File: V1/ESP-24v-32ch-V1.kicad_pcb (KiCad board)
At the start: 2 copper layers, 193 x 67.8 mm, 450 parts, among them J1 Conn_01x08, J10 USB, J11 ETHERNET, J2 Conn_01x08, J3 Conn_01x08, J4 Conn_01x08, J5 Conn_01x08, J6 Conn_01x08, J7 Conn_01x08, J8 Conn_01x08, J9 VIN, Q1 WPM2015-3/TR, Q10 MMBT2222A/SOT-23-3, Q11 MMBT2222A/SOT-23-3, Q12 MMBT2222A/SOT-23-3, Q13 MMBT2222A/SOT-23-3, Q14 MMBT2222A/SOT-23-3, Q15 MMBT2222A/SOT-23-3, Q16 MMBT2222A/SOT-23-3, Q17 MMBT2222A/SOT-23-3, Q18 MMBT2222A/SOT-23-3, Q19 MMBT2222A/SOT-23-3, Q2 LMUN2211LT1G, Q20 MMBT2222A/SOT-23-3, Q21 MMBT2222A/SOT-23-3, Q22 MMBT2222A/SOT-23-3, Q23 MMBT2222A/SOT-23-3, Q24 MMBT2222A/SOT-23-3, Q25 MMBT2222A/SOT-23-3, Q26 MMBT2222A/SOT-23-3, Q27 MMBT2222A/SOT-23-3, Q28 MMBT2222A/SOT-23-3, Q29 MMBT2222A/SOT-23-3, Q3 UMH3N, Q30 MMBT2222A/SOT-23-3, Q31 MMBT2222A/SOT-23-3, Q32 MMBT2222A/SOT-23-3, Q33 MMBT2222A/SOT-23-3, Q34 MMBT2222A/SOT-23-3, Q35 MMBT2222A/SOT-23-3, Q4 MMBT2222A/SOT-23-3, Q5 MMBT2222A/SOT-23-3, Q6 MMBT2222A/SOT-23-3, Q7 MMBT2222A/SOT-23-3, Q8 MMBT2222A/SOT-23-3, Q9 MMBT2222A/SOT-23-3, SW1 RESET, U1 SY8089A1AAC, U10 OR-3H4-4, U11 OR-3H4-4, U12 OR-3H4-4, U13 OR-3H4-4, U14 OR-3H4-4, U15 OR-3H4-4, U16 OR-3H4-4, U17 OR-3H4-4, U2 TX4138, U3 CH340C, U4 ESP32-WROOM-32UE-N16, U5 LAN8710A, U6 MCP23017_SS, U7 MCP23017_SS, U8 MCP23017_SS, U9 MCP23017_SS

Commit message: Dev
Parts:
- added REF**: OSHW-Logo2_9.8x8mm_SilkScreen, Symbol:OSHW-Logo2_9.8x8mm_SilkScreen, F.Cu at (172.7, 78.1)
- C1, C5: value 10uF/16V/1206 -> 10uF/50V/1206
- C11, C16, C17, C6, C9: value 10uF/6,3V/0603 -> 10uF/10V/0603
- C13: value 1uF/10V/0603 -> 1uF/50V/0603
- C15, C18, C19, C20: value 0,1uF/16V/0402 -> 0,1uF/50V/0402
- C21: value 1uF/6,3V/0402 -> 1uF/25V/0402
- C22: value 470pF/16V/0402 -> 470pF/50V/0402

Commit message: Replaced connector footprints
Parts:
- J1, J2, J3, J4, J5, J6, J7, J8: footprint Tales:TerminalBlock_Dorabo_DB141V-2.54-08P_1x08_P2.54mm_Vertical -> Tales:TerminalBlock_DG141V-2.54-8P_1x08_P2.54mm_Vertical

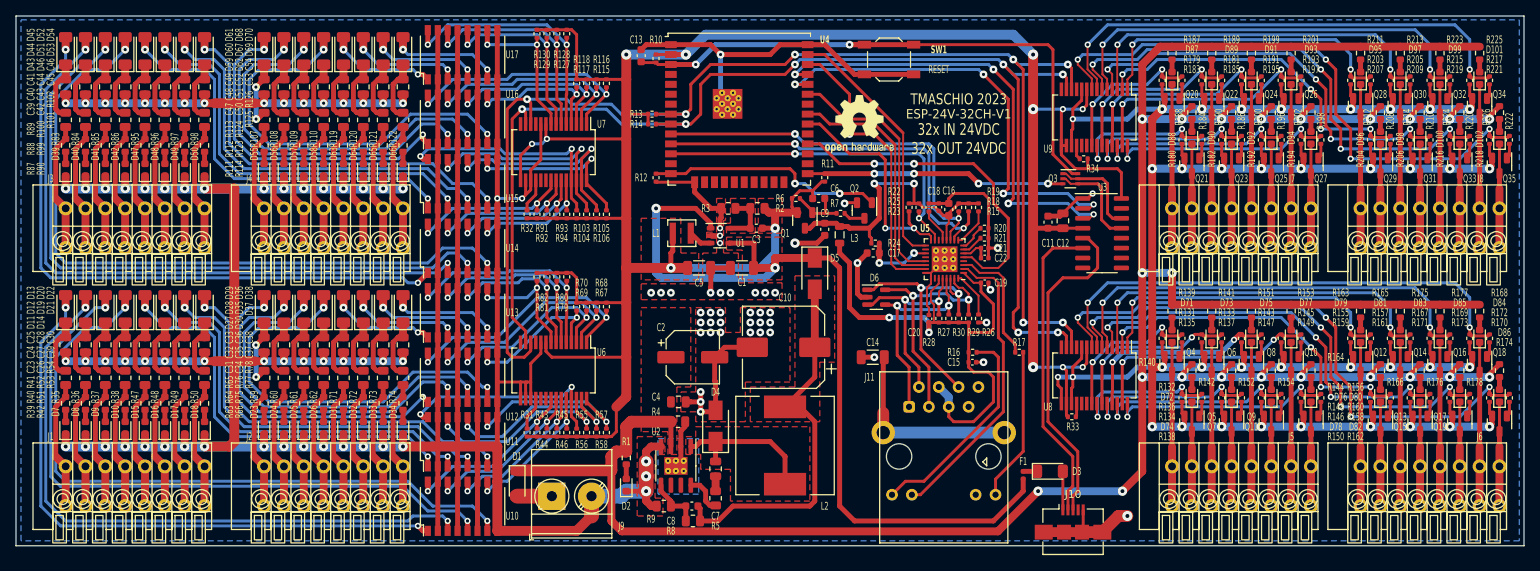
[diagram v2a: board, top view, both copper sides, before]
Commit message: Connectors rotated 180deg
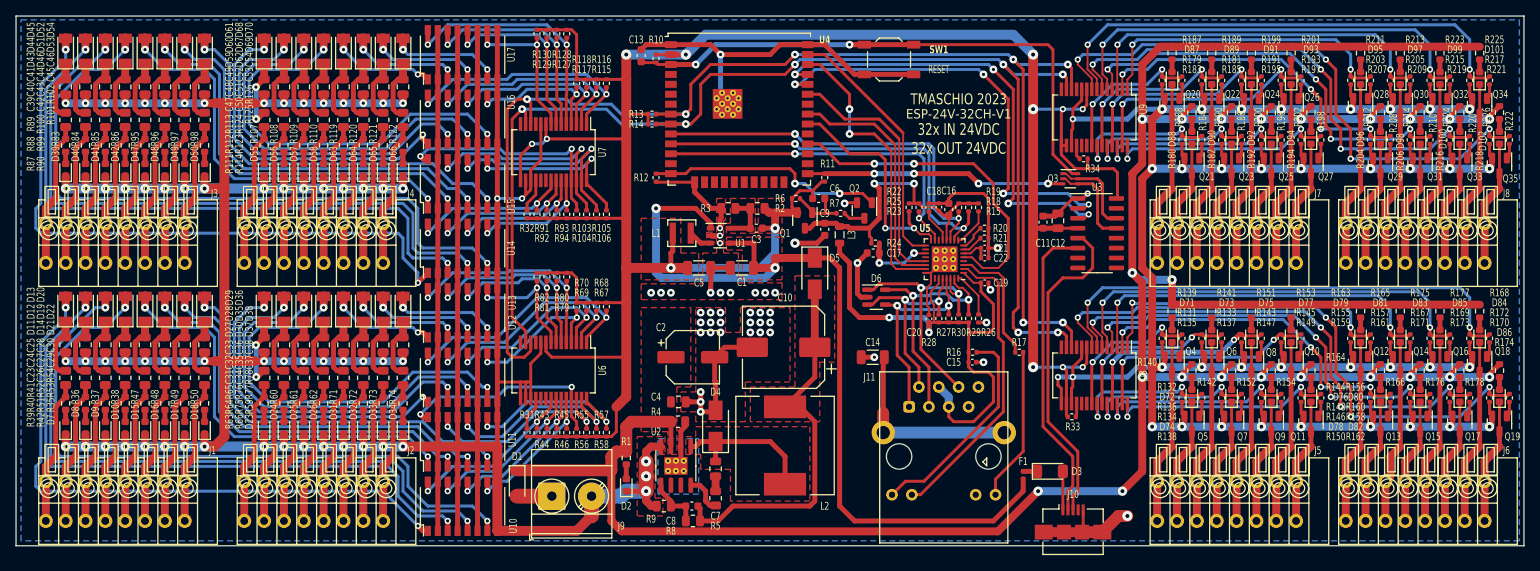
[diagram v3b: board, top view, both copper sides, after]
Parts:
- removed REF**: OSHW-Logo2_9.8x8mm_SilkScreen, Symbol:OSHW-Logo2_9.8x8mm_SilkScreen
- D11, D12, D13, D14, D19, D20, D21, D22, D27, D28, D29, D30, D35, D36, D37, D38, D43, D44, D45, D46, D51, D52, D53, D54, D59, D60, D61, D62, D67, D68, D69, D70: footprint Diode_SMD:D_MiniMELF -> Tales:D_MiniMELF
- D6: footprint Package_TO_SOT_SMD:SOT-23-5 -> Tales:SOT-23-5
- J1, J2, J3, J4, J5, J6, J7, J8: footprint Tales:TerminalBlock_DG141V-2.54-8P_1x08_P2.54mm_Vertical -> Tales:TerminalBlock_Phoenix_FFKDSA1-V-2.54-8_1x08_P2.54mm_Vertical
- L3: footprint Inductor_SMD:L_0805_2012Metric -> Tales:L_0805_2012Metric
- U10, U11, U12, U13, U14, U15, U16, U17: footprint Package_SO:SOP-16_4.4x10.4mm_P1.27mm -> Tales:SOP-16_4.4x10.4mm_P1.27mm
- U3: footprint Package_SO:SOIC-16_3.9x9.9mm_P1.27mm -> Tales:SOIC-16_3.9x9.9mm_P1.27mm
- U6, U7, U8, U9: footprint Package_SO:SSOP-28_5.3x10.2mm_P0.65mm -> Tales:SSOP-28_5.3x10.2mm_P0.65mm
- moved J1 3.18 mm to (68.6, 128.9)
- moved J3 3.18 mm to (68.6, 95.9)
- moved J2 3.17 mm to (94.0, 128.9)
- moved J4 3.17 mm to (94.0, 95.9)
- moved J5 2.69 mm to (210.8, 128.9)
- moved J6 2.69 mm to (234.9, 128.9)
- moved J7 2.69 mm to (210.8, 95.9)
- moved J8 2.69 mm to (234.9, 95.9)
- moved U3 0.64 mm to (203.1, 92.1)
- moved C11 0.63 mm to (196.2, 90.7)
- moved C12 0.63 mm to (198.1, 90.5)
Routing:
- net GND: track 1146.6 -> 1155.7 mm
- net Net-(D46-A): track 91.4 -> 88.0 mm
- net Net-(D45-A): track 88.4 -> 84.9 mm
- net Net-(D44-A): track 84.8 -> 81.8 mm
- net /Outputs 17-32/J11-OUT32: track 13.3 -> 16.0 mm
- net /Outputs 17-32/J11-OUT31: track 21.0 -> 23.6 mm
- net /Outputs 17-32/J11-OUT30: track 13.3 -> 16.0 mm
- net /Outputs 17-32/J11-OUT28: track 13.3 -> 16.0 mm
- net /Outputs 17-32/J11-OUT27: track 21.0 -> 23.6 mm
- net /Outputs 17-32/J11-OUT26: track 13.3 -> 16.0 mm
- net /Outputs 17-32/J11-OUT25: track 21.0 -> 23.6 mm
- net /Outputs 17-32/J10-OUT24: track 13.3 -> 16.0 mm
- net /Outputs 17-32/J10-OUT23: track 21.0 -> 23.6 mm
- net /Outputs 17-32/J10-OUT22: track 13.3 -> 16.0 mm
- net /Outputs 17-32/J10-OUT21: track 21.0 -> 23.6 mm
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
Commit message: Connector rotated 180deg
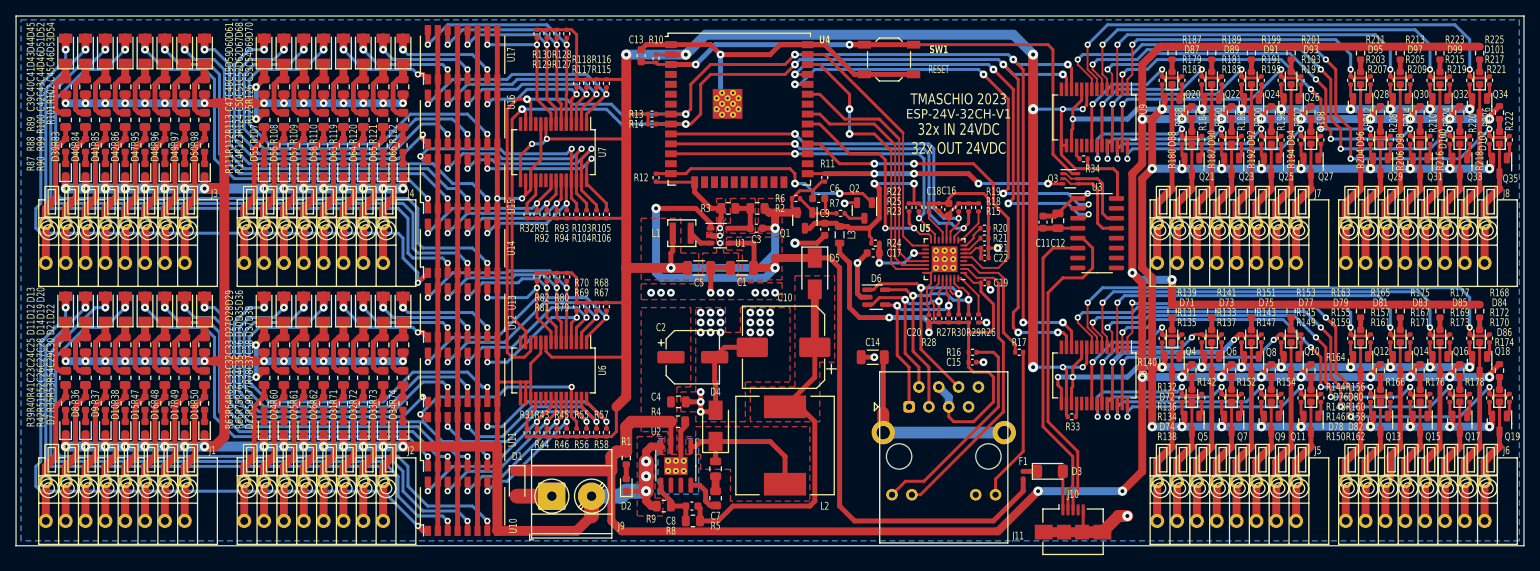
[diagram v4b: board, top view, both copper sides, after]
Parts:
- turned J11 to 0 degrees
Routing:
- net Net-(D5-A): track 49.1 -> 47.2 mm
- net GND: track 1155.7 -> 1153.8 mm
- net /GPIO Expanders/IN9: track 33.7 -> 33.0 mm
- net /MCU/USB_D+: track 41.6 -> 41.0 mm
